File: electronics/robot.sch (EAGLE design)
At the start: 24 parts, among them U1 MT3608

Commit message: Removing former directories (electronics merged)
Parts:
- removed C12: 22uF, resistor:C-EUC0805
- removed C9: (no value), rcl:CPOL-EU153CLV-1010
- removed D2: PMEG4030EP, nxp_60:PMEG4030EP
- removed MOS: SUD50N04-8M8P-4GE3, rhoban:SUD50N04-8M8P-4GE3
- removed U$1, U$2, U$3, U$4, U$5: CONNEC_1X01PAD, rhoban:CONNEC_1X01PAD
- added B1: BUZZER66, rhoban:BUZZER66
- added C11: 47pF, SparkFun-Passives:CAP0805
- added C15, C16: 22uF, resistor:C-EUC0805
- added C19, C20: 2200uF, rcl:CPOL-EUE5-13
- added D1: PMEG4030EP, nxp_60:PMEG4030EP
- added D3: (no value), SparkFun-DiscreteSemi:DIODESOD
- added J1: USB-B, SparkFun-Connectors:USBPTH
- added J2: DC21MMX, powersupply:DC21MMX
- added J3, J4, J5: B6B-ZR, jst:B6B-ZR
- added J6: KICKER, rhoban:KICKER
- added LED1, LED2, LED3, LED4, LED5, LED6: WS2812B5050, adafruit:WS2812B5050
- added Q1, Q2: IRLMS2002TRPBF, rhoban:IRLMS2002TRPBF
- added Q3: NPN_BC817,215, rhoban:NPN_BC817,215
- added Q4: SUD50N04-8M8P-4GE3, rhoban:SUD50N04-8M8P-4GE3
- added R10, R5, R9: 10K, SparkFun-Resistors:0.3OHM-0805-1/8W-1%
- added R11, R8: 2K, SparkFun-Resistors:0.3OHM-0805-1/8W-1%
- added R12, R13: 22, SparkFun-Resistors:0.3OHM-0805-1/8W-1%
- added R6: 0.3OHM-0805-1/8W-1%, SparkFun-Resistors:0.3OHM-0805-1/8W-1%
- added R7: 470, SparkFun-Resistors:0.3OHM-0805-1/8W-1%
- added REG1, REG2: REG_5V, rhoban:REG_5V
- added S1: DPDT, rhoban:DPDT
- added U2: ESP32-WROOM-32E_(16MB), ESP32-WROOM-32E__16MB_:ESP32-WROOM-32E_(16MB)
- added U3: S8252, rhoban:S8252
- added U4, U5, U6: L9110, rhoban:L9110
- added U7: MT3608, MT3608:MT3608
- C1, C4, C7: value (none) -> 0.1µF; device rcl:CPOL-EU153CLV-1010 -> SparkFun-Capacitors:0.33UF/330NF-0805-50V-10%; FARNELL 2610827 -> 2688486RL
- C10: value 22uF -> 47pF; device resistor:C-EUC0805 -> SparkFun-Passives:CAP0805; FARNELL 2611932 -> 1081223
- C2, C3, C5, C6, C8: value (none) -> 0.1µF; device rcl:CPOL-EU153CLV-1010 -> SparkFun-Capacitors:0.33UF/330NF-0805-50V-10%; FARNELL 2610827 -> 2688486RL; PROD_ID (none) -> CAP-08469; VALUE (none) -> 0.33µF
- R1: value (none) -> 270; device rcl:R-EU_R2010 -> SparkFun-Resistors:0.3OHM-0805-1/8W-1%
- R2: device resistor:R-EU_M0805 -> SparkFun-Resistors:0.3OHM-0805-1/8W-1%; FARNELL (none) -> MCWR08X2001FTL
- R3: value (none) -> 20K; device resistor:R-EU_M0805 -> SparkFun-Resistors:0.3OHM-0805-1/8W-1%; FARNELL (none) -> 2074395
- R4: device resistor:R-EU_M0805 -> SparkFun-Resistors:0.3OHM-0805-1/8W-1%
- U1: value MT3608 -> FT232L; device MT3608:MT3608 -> rhoban:FT232L; FARNELL (none) -> 1146032
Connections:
- new net 3.3: B1.P$2, J3.2, J4.2, J5.2
- new net 3.3V: REG2.OUT, U1.VCC, U1.VCCIO, U2.3V3
- new net BUZZER: R8.2, U2.IO32
- new net GND_RAW: C7.2, C8.1, J2.3, Q1.S, R10.2, S1.P$5, U3.VSS
- new net LEDS: LED1.DI, U2.IO27
- new net LEDS_SUITE: LED6.DO
- new net M1A: U2.IO13, U4.IA
- new net M1B: U2.IO14, U4.IB
- new net M1C1: J3.4, U2.IO15
- new net M1C2: J3.3, U2.IO16
- new net M1P1: J3.6, U4.OA
- new net M1P2: J3.1, U4.OB
- new net M2A: U2.IO17, U5.IA
- new net M2B: U2.IO18, U5.IB
- new net M2C1: J4.4, U2.IO19
- new net M2C2: J4.3, U2.IO21
- new net M2P1: J4.6, U5.OA
- new net M2P2: J4.1, U5.OB
- new net M3A: U2.IO22, U6.IA
- new net M3B: U2.IO23, U6.IB
- new net M3C1: J5.4, U2.IO25
- new net M3C2: J5.3, U2.IO26
- new net M3P1: J5.6, U6.OA
- new net M3P2: J5.1, U6.OB
- new net N$10: Q1.D, Q2.D
- new net N$11: Q2.G, U3.CO
- new net N$12: Q1.G, U3.DO
- new net N$13: R11.1, S1.P$2, U3.VM
- new net N$14: U1.TXD, U2.TXD0
- new net N$15: U1.RXD, U2.RXD0
- new net N$27: LED1.DO, LED2.DI
- new net N$28: LED2.DO, LED3.DI
- new net N$30: LED4.DO, LED5.DI
- new net N$32: LED5.DO, LED6.DI
- new net N$39: LED3.DO, LED4.DI
- new net N$4: R2.2, R4.1, U7.FB
- new net N$5: B1.P$1, Q3.C
- new net N$59: J1.D-, R12.1
- new net N$60: J1.D+, R13.1
- new net N$7: J2.2, S1.P$1
- new net N$8: C8.2, R7.1, U3.VDD
- new net N$9: C7.1, R10.1, R9.2, U3.VC
- new net USBDM: C10.2, R12.2, U1.USBDM
- new net USBDP: C11.2, R13.2, U1.USBDP
- new net VCC: C4.1, C5.1, C6.1, D3.C, LED1.VDD, LED2.VDD, LED3.VDD, LED4.VDD, LED5.VDD, LED6.VDD, REG1.OUT
- new net VOLTAGE: R3.1, R5.2, U2.IO34
- new net VUSB: D3.A, J1.VBUS
- net GND: now also C1.2, C10.1, C11.1, C15.2, C16.2, C19.-, C2.2, C20.-, C3.2, C4.2, C5.2, C6.2, J1.GND, J3.5, J4.5, J5.5, LED1.GND, LED2.GND, LED3.GND, LED4.GND, LED5.GND, LED6.GND, Q2.S, Q3.E, Q4.S, R11.2, R5.1, R6.2, REG1.GND, REG2.GND, U1.GND@1, U1.GND@2, U1.GND@A, U2.GND, U4.GND, U5.GND, U6.GND, U7.GND; no longer C1.-, C10.2, C12.2, C2.-, C3.-, C4.-, C5.-, C6.-, C7.-, C8.-, C9.-, MOS.S, R3.2, U$1.1
- net KICK: now also Q4.G, R6.1, U2.IO33; no longer MOS.G, R3.1, U$3.1
- net KICKER: now also J6.2, Q4.D; no longer MOS.D, U$5.1
- net N$1: now also D1.A, U7.SW; no longer D2.A, U1.SW
- net N$2: now also C16.1, D1.K; no longer C10.1, D2.K
- net N$3: now also Q3.B, R8.1; no longer R2.2, R4.1, U1.FB
- net VIN: now also C1.1, C15.1, C2.1, C3.1, R3.2, R7.2, R9.1, REG1.IN, REG2.IN, S1.P$4, U4.VCC, U5.VCC, U6.VCC, U7.EN, U7.IN; no longer C12.1, U$2.1, U1.EN, U1.IN
- net VSTORE: now also C19.+, C20.+, J6.1; no longer C1.+, C2.+, C3.+, C4.+, C5.+, C6.+, C7.+, C8.+, C9.+, U$4.1
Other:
- note added: "BMS cut at 0.2V, so ~3.3A"
- note added: "BUZZER"
- note added: "H BRIDGES"
- note added: "LEDS"
- note added: "POWER"
- note added: "RDSon is ~30 mohm. So "Rsense" is 60mohm"

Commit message: BOM
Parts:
- J6: FARNELL (none) -> JF-0530B
- R2: FARNELL MCWR08X2001FTL -> 2447622
- U2: FARNELL (none) -> ESP32-WROOM
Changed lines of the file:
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@@
 </part>
 <part name="R2" library="SparkFun-Resistors" deviceset="0.3OHM" device="-0805-1/8W-1%" value="2k">
-<attribute name="FARNELL" value="MCWR08X2001FTL"/>
+<attribute name="FARNELL" value="2447622"/>
 </part>
 <part name="R6" library="SparkFun-Resistors" deviceset="0.3OHM" device="-0805-1/8W-1%">
@@
 <attribute name="FARNELL" value="1829201 "/>
 </part>
-<part name="U2" library="ESP32-WROOM-32E__16MB_" deviceset="ESP32-WROOM-32E_(16MB)" device=""/>
+<part name="U2" library="ESP32-WROOM-32E__16MB_" deviceset="ESP32-WROOM-32E_(16MB)" device="">
+<attribute name="FARNELL" value="ESP32-WROOM"/>
+</part>
 <part name="U3" library="rhoban" deviceset="S8252" device="">
 <attribute name="FARNELL" value="https://www.digikey.fr/fr/products/detail/ablic-u-s-a-inc/S-8252AAL-M6T1U/6121452"/>
@@
 <attribute name="FARNELL" value="1146032"/>
 </part>
-<part name="J6" library="rhoban" deviceset="KICKER" device=""/>
+<part name="J6" library="rhoban" deviceset="KICKER" device="">
+<attribute name="FARNELL" value="JF-0530B"/>
+</part>
 <part name="C19" library="rcl" deviceset="CPOL-EU" device="E5-13" value="2200uF">
 <attribute name="FARNELL" value="1902893"/>
@@
 <attribute name="FARNELL" x="-119.38" y="7.62" size="1.778" layer="96" rot="R180" display="off"/>
 </instance>
-<instance part="U2" gate="G$1" x="40.64" y="-20.32"/>
+<instance part="U2" gate="G$1" x="40.64" y="-20.32">
+<attribute name="FARNELL" x="40.64" y="-20.32" size="1.778" layer="96" display="off"/>
+</instance>
 <instance part="U1" gate="1" x="-33.02" y="-15.24">
 <attribute name="FARNELL" x="-33.02" y="-15.24" size="1.778" layer="96" display="off"/>
@@
 <attribute name="FARNELL" x="2.54" y="12.7" size="1.778" layer="96" display="off"/>
 </instance>
-<instance part="J6" gate="A" x="104.14" y="-10.16"/>
+<instance part="J6" gate="A" x="104.14" y="-10.16">
+<attribute name="FARNELL" x="104.14" y="-10.16" size="1.778" layer="96" display="off"/>
+</instance>
 <instance part="C19" gate="G$1" x="40.64" y="-17.78">
 <attribute name="FARNELL" x="40.64" y="-17.78" size="1.778" layer="96" display="off"/>

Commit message: Autorouting to test
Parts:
- removed D3: (no value), SparkFun-DiscreteSemi:DIODESOD
- removed R1: 270, SparkFun-Resistors:0.3OHM-0805-1/8W-1%
- added C9: 0.1µF, SparkFun-Capacitors:0.33UF/330NF-0805-50V-10%
- added R14: 270, rcl:R-EU_R2010
- C19, C20: FARNELL 1902893 -> 2749341
- R6: value 0.3OHM-0805-1/8W-1% -> 3K; FARNELL 2447648 -> 1887603; PROD_ID (none) -> RES-11622; VALUE (none) -> 0.3
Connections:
- removed net VUSB: D3.A, J1.VBUS
- new net N$6: U1.TXD, U2.RXD0
- net GND: now also C9.2, R6.1; no longer R6.2
- net KICK: now also R6.2; no longer R6.1
- net N$14: now also U1.RXD; no longer U1.TXD
- net N$15: now also C9.1, U1.3V3OUT; no longer U1.RXD, U2.RXD0
- net N$2: now also R14.2; no longer R1.2
- net VCC: now also J1.VBUS, REG2.IN; no longer D3.C
- net VIN: no longer REG2.IN
- net VSTORE: now also R14.1; no longer R1.1
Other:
- moved on the sheet: R6

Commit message: BMS resistors
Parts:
- R10, R9: value 10K -> 470
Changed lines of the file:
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@@
 <attribute name="FARNELL" value="2447662"/>
 </part>
-<part name="R9" library="SparkFun-Resistors" deviceset="0.3OHM" device="-0805-1/8W-1%" value="10K">
+<part name="R9" library="SparkFun-Resistors" deviceset="0.3OHM" device="-0805-1/8W-1%" value="470">
 <attribute name="FARNELL" value="2074334RL"/>
 </part>
-<part name="R10" library="SparkFun-Resistors" deviceset="0.3OHM" device="-0805-1/8W-1%" value="10K">
+<part name="R10" library="SparkFun-Resistors" deviceset="0.3OHM" device="-0805-1/8W-1%" value="470">
 <attribute name="FARNELL" value="2074334RL"/>
 </part>

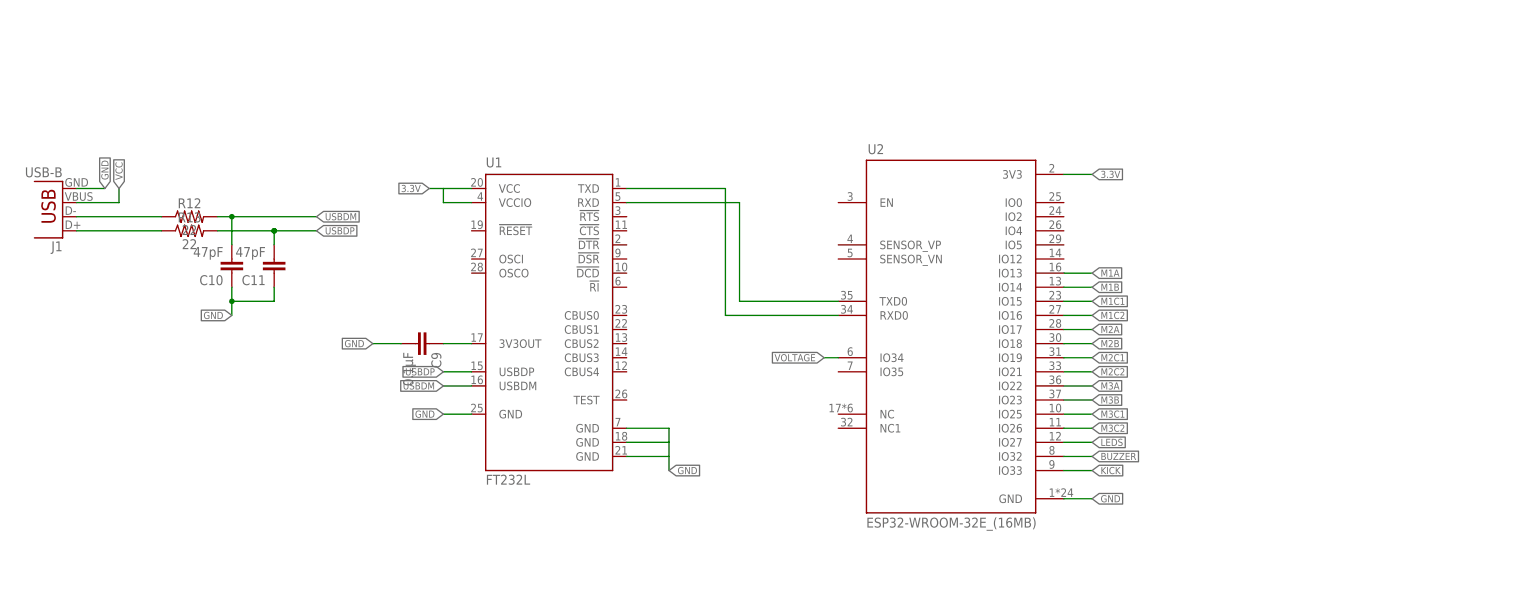
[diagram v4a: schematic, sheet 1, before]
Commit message: DTR/RTS ESP programming and fixes
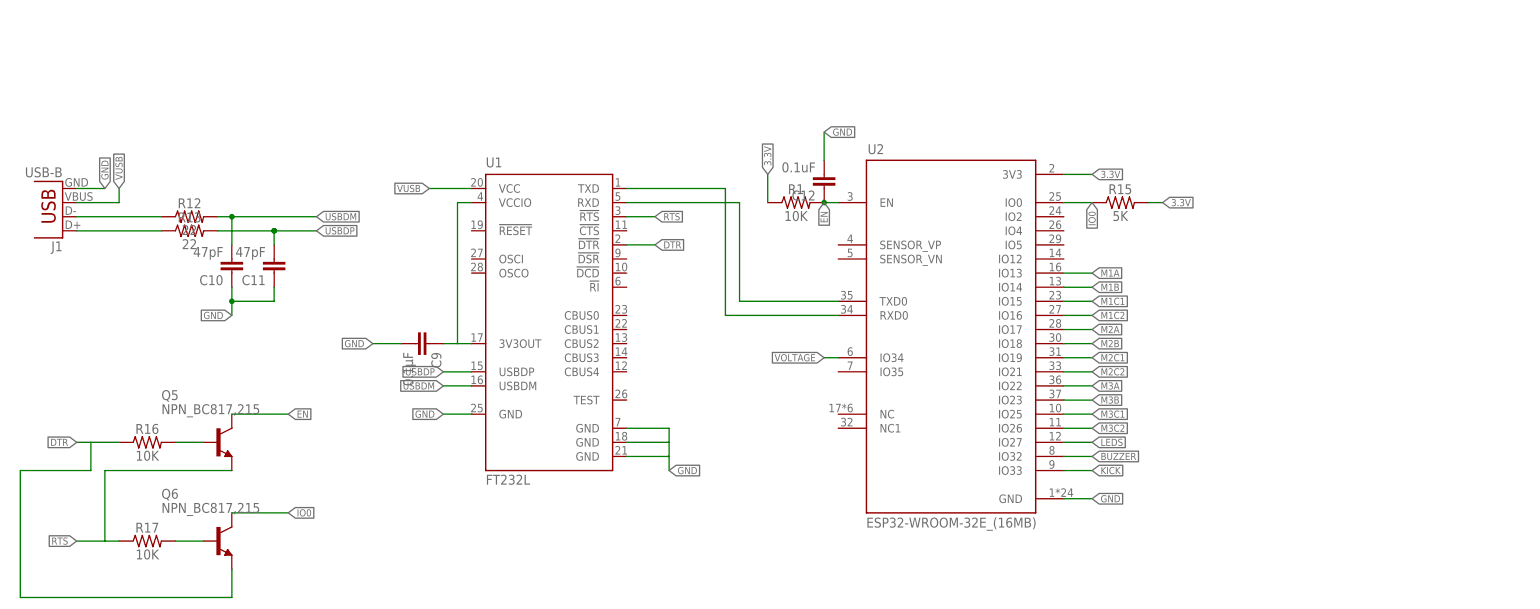
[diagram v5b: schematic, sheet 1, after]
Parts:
- removed REG2: REG_5V, rhoban:REG_5V
- added C12: 0.1uF, SparkFun-Passives:CAP0805
- added C13: 1 µF, SparkFun-Capacitors:0.33UF/330NF-0805-50V-10%
- added C14: 0.1µF, SparkFun-Capacitors:0.33UF/330NF-0805-50V-10%
- added D3: (no value), SparkFun-DiscreteSemi:DIODESOD
- added Q5, Q6: NPN_BC817,215, rhoban:NPN_BC817,215
- added R1, R16, R17: 10K, SparkFun-Resistors:0.3OHM-0805-1/8W-1%
- added R15: 5K, SparkFun-Resistors:0.3OHM-0805-1/8W-1%
- added U$25: TS2940CW-3.3RP, rhoban:TS2940CW-3.3RP
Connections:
- removed net 3.3: B1.P$2, J3.2, J4.2, J5.2
- new net DTR: Q6.E, R16.1, U1.!DTR
- new net EN: C12.1, Q5.C, R1.2, U2.EN
- new net IO0: Q6.C, R15.1, U2.IO0
- new net N$16: Q5.B, R16.2
- new net N$17: Q6.B, R17.2
- new net RTS: Q5.E, R17.1, U1.!RTS
- new net VUSB: D3.A, J1.VBUS, U1.VCC
- net 3.3V: now also B1.P$2, C13.1, C14.1, J3.2, J4.2, J5.2, R1.1, R15.2, U$25.OUT; no longer REG2.OUT, U1.VCC, U1.VCCIO
- net GND: now also C12.2, C13.2, C14.2, U$25.GND; no longer REG2.GND
- net N$15: now also U1.VCCIO
- net VCC: now also D3.C, U$25.IN; no longer J1.VBUS, REG2.IN
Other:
- note added: "USB & ESP32"

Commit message: Minor fixes
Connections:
- removed net LEDS_SUITE: LED6.DO
- net GND: now also U1.TEST
- net M1C1: now also U2.IO4; no longer U2.IO15
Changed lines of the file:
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@@
 <wire x1="-17.78" y1="-40.64" x2="-10.16" y2="-40.64" width="0.1524" layer="91"/>
 <label x="-10.16" y="-43.18" size="1.27" layer="95" xref="yes"/>
+<pinref part="U1" gate="1" pin="TEST"/>
+<wire x1="-17.78" y1="-30.48" x2="-10.16" y2="-30.48" width="0.1524" layer="91"/>
+<wire x1="-10.16" y1="-30.48" x2="-10.16" y2="-35.56" width="0.1524" layer="91"/>
 </segment>
 <segment>
@@
 <net name="M1C1" class="0">
 <segment>
-<pinref part="U2" gate="G$1" pin="IO15"/>
-<wire x1="60.96" y1="-12.7" x2="66.04" y2="-12.7" width="0.1524" layer="91"/>
-<label x="66.04" y="-12.7" size="1.27" layer="95" xref="yes"/>
+<pinref part="U2" gate="G$1" pin="IO4"/>
+<wire x1="60.96" y1="0" x2="66.04" y2="0" width="0.1524" layer="91"/>
+<label x="66.04" y="0" size="1.27" layer="95" xref="yes"/>
 </segment>
 </net>
@@
 </segment>
 </net>
-<net name="LEDS_SUITE" class="0">
-<segment>
-<pinref part="LED6" gate="G$1" pin="DO"/>
-<wire x1="96.52" y1="-5.08" x2="104.14" y2="-5.08" width="0.1524" layer="91"/>
-<label x="104.14" y="-5.08" size="1.27" layer="95" xref="yes"/>
-</segment>
-</net>

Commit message: rev0
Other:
- moved on the sheet: C5, C6
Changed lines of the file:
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@@
 <attribute name="FARNELL" x="-55.88" y="22.86" size="1.778" layer="96" display="off"/>
 </instance>
-<instance part="C5" gate="G$1" x="5.08" y="20.32">
-<attribute name="FARNELL" x="5.08" y="20.32" size="1.778" layer="96" display="off"/>
+<instance part="C5" gate="G$1" x="10.16" y="22.86">
+<attribute name="FARNELL" x="10.16" y="22.86" size="1.778" layer="96" display="off"/>
 </instance>
-<instance part="C6" gate="G$1" x="71.12" y="17.78">
-<attribute name="FARNELL" x="71.12" y="17.78" size="1.778" layer="96" display="off"/>
+<instance part="C6" gate="G$1" x="73.66" y="22.86">
+<attribute name="FARNELL" x="73.66" y="22.86" size="1.778" layer="96" display="off"/>
 </instance>
 </instances>
@@
 </segment>
 <segment>
-<wire x1="5.08" y1="17.78" x2="5.08" y2="12.7" width="0.1524" layer="91"/>
-<label x="5.08" y="12.7" size="1.27" layer="95" xref="yes"/>
+<wire x1="10.16" y1="20.32" x2="10.16" y2="15.24" width="0.1524" layer="91"/>
+<label x="10.16" y="15.24" size="1.27" layer="95" xref="yes"/>
 <pinref part="C5" gate="G$1" pin="2"/>
 </segment>
 <segment>
-<wire x1="71.12" y1="15.24" x2="71.12" y2="10.16" width="0.1524" layer="91"/>
-<label x="71.12" y="10.16" size="1.27" layer="95" xref="yes"/>
+<wire x1="73.66" y1="20.32" x2="73.66" y2="15.24" width="0.1524" layer="91"/>
+<label x="73.66" y="15.24" size="1.27" layer="95" xref="yes"/>
 <pinref part="C6" gate="G$1" pin="2"/>
 </segment>
@@
 </segment>
 <segment>
-<wire x1="5.08" y1="25.4" x2="5.08" y2="30.48" width="0.1524" layer="91"/>
-<label x="5.08" y="30.48" size="1.27" layer="95" xref="yes"/>
+<wire x1="10.16" y1="27.94" x2="10.16" y2="33.02" width="0.1524" layer="91"/>
+<label x="10.16" y="33.02" size="1.27" layer="95" xref="yes"/>
 <pinref part="C5" gate="G$1" pin="1"/>
 </segment>
@@
 </segment>
 <segment>
-<wire x1="71.12" y1="22.86" x2="71.12" y2="27.94" width="0.1524" layer="91"/>
-<label x="71.12" y="27.94" size="1.27" layer="95" xref="yes"/>
+<wire x1="73.66" y1="27.94" x2="73.66" y2="33.02" width="0.1524" layer="91"/>
+<label x="73.66" y="33.02" size="1.27" layer="95" xref="yes"/>
 <pinref part="C6" gate="G$1" pin="1"/>
 </segment>

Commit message: Electronic fixes
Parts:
- removed S1: DPDT, rhoban:DPDT
- added C17: 1µF, SparkFun-Capacitors:0.33UF/330NF-0805-50V-10%
- added Q7: IRLMS2002TRPBF, rhoban:IRLMS2002TRPBF
- added R18: 56K, SparkFun-Resistors:0.3OHM-0805-1/8W-1%
- added U$1: L102011ML04Q, rhoban:L102011ML04Q
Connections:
- new net N$19: C17.2, Q7.G, R18.2
- net GND_RAW: now also Q7.S, R18.1; no longer S1.P$5
- net N$13: now also Q7.D; no longer S1.P$2
- net N$7: now also U$1.COM; no longer S1.P$1
- net VIN: now also C17.1, U$1.A; no longer S1.P$4
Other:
- moved on the sheet: C13, C14, D3
